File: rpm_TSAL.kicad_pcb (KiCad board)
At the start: 4 copper layers, 123 parts, among them J1 Conn_01x02, J14 Conn_01x04, J2 Conn_01x04, J3 Conn_01x04, J4 Conn_01x04, J6 Conn_01x02, J7 Conn_01x02, Q1 NMOS, Q2 NMOS, Q3 NMOS, Q4 NMOS, Q5 PMOS, Q7 NMOS, U1 OPA355NA, U10 SN74HCS266PWR, U11 OPA355NA, U12 74LVC1G32GV, U13 SFH617A-1X007T, U14 OPA355NA, U15 TBA1-1211E, U16 TBA1-0511E, U17 TBA1-0511E, U18 IP4252CZ16, U2 L7805, U3 74LVC2G74, U4 SFH617A-1X007T, U5 NE555D, U6 CD74HC30PWR, U7 4072, U8 4001, U9 74LVC1G32GV

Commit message: Added Sub project
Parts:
- removed C2, C36, C38, C5, C6, C7: 100nF, Capacitor_SMD:C_0603_1608Metric
- removed C35, C37: 10uF, Capacitor_SMD:C_0603_1608Metric
- removed Q7: NMOS, Package_TO_SOT_SMD:SOT-23-3
- removed R1, R22, R23, R25, R26, R67: 1k, Resistor_SMD:R_0603_1608Metric
- removed R2, R3, R4, R5, R6, R7: 52k3, Resistor_SMD:R_0805_2012Metric
- removed R24: 12k, Resistor_SMD:R_0603_1608Metric
- removed R27, R83: 10k, Resistor_SMD:R_0603_1608Metric
- removed R82: 200R, Resistor_SMD:R_0603_1608Metric
- removed U1: OPA355NA, Package_TO_SOT_SMD:SOT-23-6
- removed U17: TBA1-0511E, Converter_DCDC:Converter_DCDC_TRACO_TBA1-xxxxE_Single_THT
- removed U4: SFH617A-1X007T, Package_DIP:SMDIP-4_W9.53mm_Clearance8mm
- removed U5: NE555D, Package_SO:SOIC-8_3.9x4.9mm_P1.27mm
- added H5: MountingHole, MountingHole:MountingHole_3.2mm_M3, F.Cu at (129.1, 76.5)
- added J10: Conn_01x10, Connector_IDC:IDC-Header_2x05_P2.54mm_Latch6.5mm_Vertical, F.Cu at (174.0, 76.2)
- H1, H2, H3, H4: footprint MountingHole:MountingHole_3.2mm_M3_DIN965 -> MountingHole:MountingHole_3.2mm_M3
- U19, U20, U21: moved to B.Cu
- moved J14 181.8 mm to (188.8, 126.0)
- moved R13 181.7 mm to (243.9, 111.7), turned to 90 degrees
- moved R12 181.4 mm to (243.9, 105.3), turned to -90 degrees
- moved R11 181.2 mm to (243.9, 99.3), turned to -90 degrees
- moved R10 181.1 mm to (243.9, 93.3), turned to 90 degrees
- moved R9 181.0 mm to (243.9, 87.3), turned to 90 degrees
- moved R8 181.0 mm to (243.9, 82.2), turned to 90 degrees
- moved C8 169.2 mm to (191.8, 101.4), turned to 90 degrees
- moved J2 168.4 mm to (154.9, 126.2)
- moved U15 168.2 mm to (198.3, 102.8)
- moved C4 168.1 mm to (189.3, 101.4), turned to 90 degrees
- moved C3 167.1 mm to (186.8, 101.4), turned to 90 degrees
- moved C1 166.1 mm to (184.3, 101.4), turned to 90 degrees
- moved C15 166.1 mm to (191.8, 97.4), turned to 90 degrees
- moved U11 166.0 mm to (232.8, 85.5), turned to 180 degrees
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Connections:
- J1 pad 1: HV+ -> HV-
- J1 pad 2: HV- -> HV+
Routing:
- net HV-: track 0.00 -> 27.2 mm
- net Net-(U11-+): track 0.00 -> 11.1 mm
- net Net-(J10-Pin_9): track 0.00 -> 8.90 mm
- net Net-(J10-Pin_3): track 0.00 -> 8.86 mm
- net Net-(J10-Pin_7): track 0.00 -> 8.23 mm
- net Net-(J10-Pin_5): track 0.00 -> 8.14 mm
- net Net-(J10-Pin_2): track 0.00 -> 6.26 mm
- net HV+: track 0.00 -> 5.70 mm
- net Net-(J10-Pin_4): track 0.00 -> 5.53 mm
- net Net-(J10-Pin_8): track 0.00 -> 5.53 mm
- net Net-(J10-Pin_6): track 0.00 -> 4.81 mm
- net Net-(R12-Pad2): track 0.00 -> 4.60 mm
- net Net-(R10-Pad2): track 0.00 -> 4.18 mm
- net Net-(R11-Pad2): track 0.00 -> 4.17 mm
- net Net-(R10-Pad1): track 0.00 -> 4.15 mm
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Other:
- board outline added: 125.3 x 61.3 mm
- board text added: "Isolating Case over LV Section"

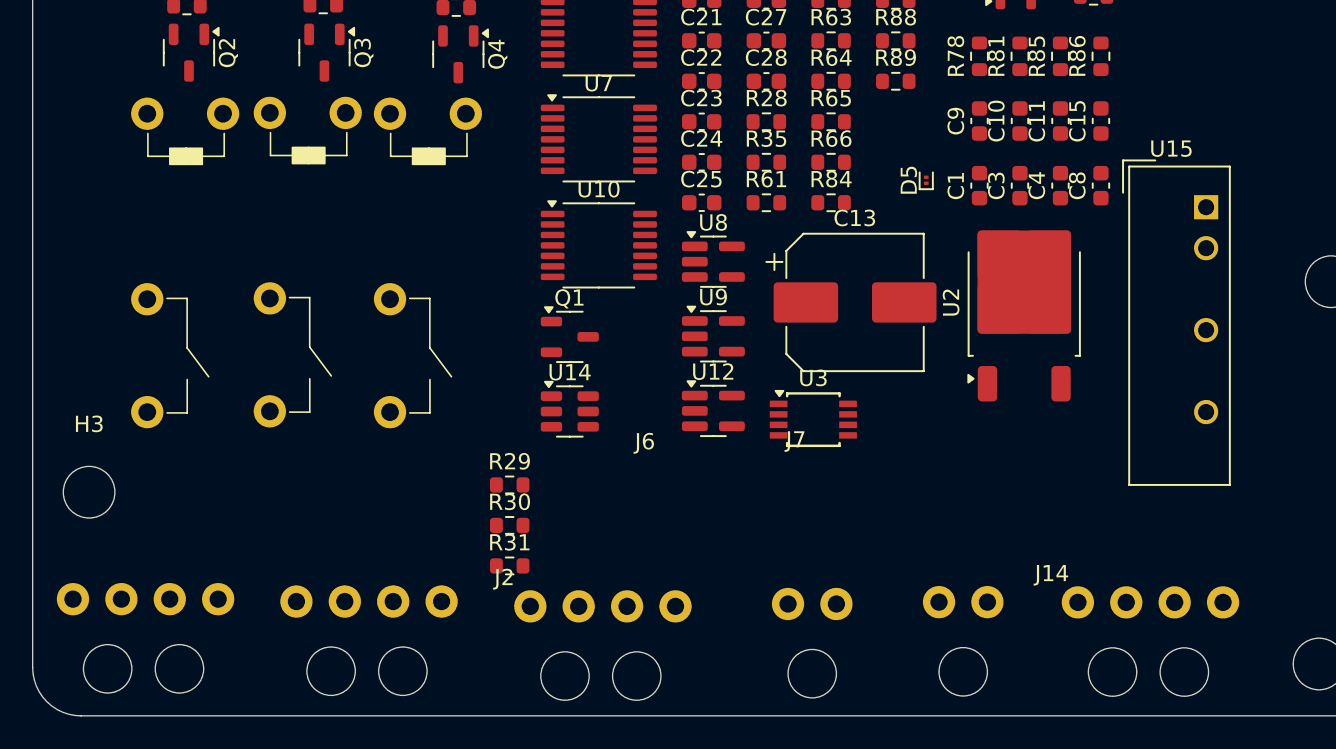
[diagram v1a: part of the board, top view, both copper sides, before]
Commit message: Connector Updated
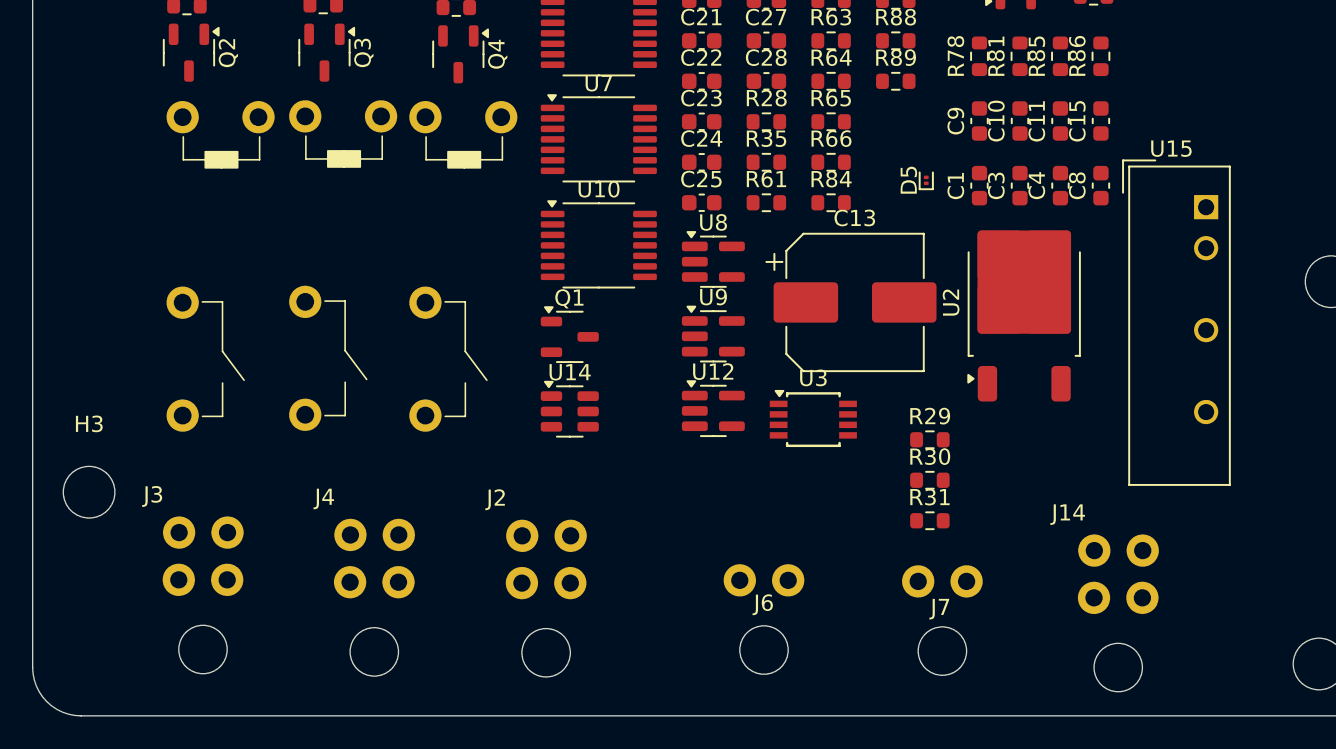
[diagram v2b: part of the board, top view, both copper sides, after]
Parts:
- J14, J2, J3, J4: footprint wuerth_conn:66200411022 -> wuerth_conn:66200421022
- moved R29 26.2 mm to (181.2, 117.2)
- moved R30 26.2 mm to (181.2, 119.7)
- moved R31 26.2 mm to (181.2, 122.2)
- moved J3 8.02 mm to (133.1, 121.2)
- moved J4 5.69 mm to (143.7, 121.3)
- moved J2 4.88 mm to (154.3, 121.4)
- moved J14 3.83 mm to (189.8, 122.3)
- moved J6 3.33 mm to (169.4, 125.9)
- moved U19 2.21 mm to (140.8, 96.2)
- moved U21 2.21 mm to (155.9, 96.2)
- moved U20 2.21 mm to (148.4, 96.1)
- moved J7 1.82 mm to (180.5, 126.0)

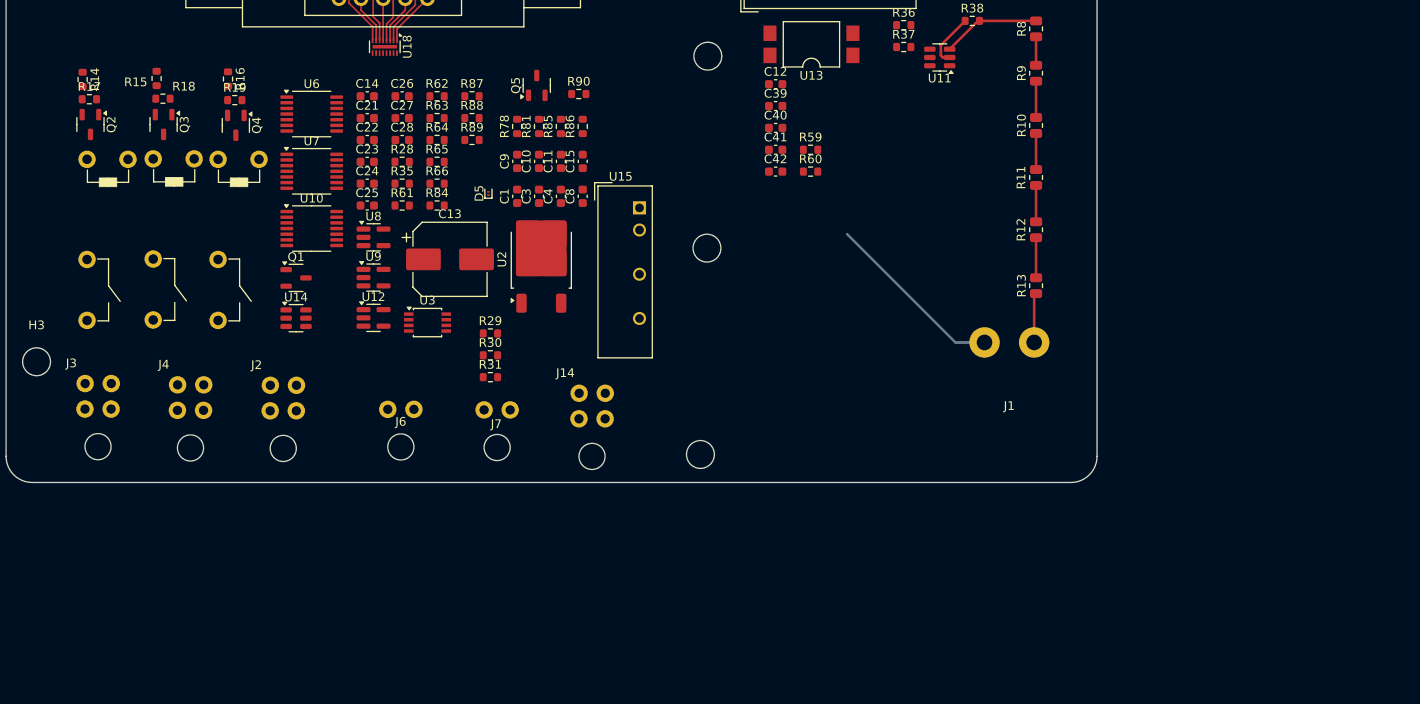
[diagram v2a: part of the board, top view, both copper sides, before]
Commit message: Routing of AIR Relay
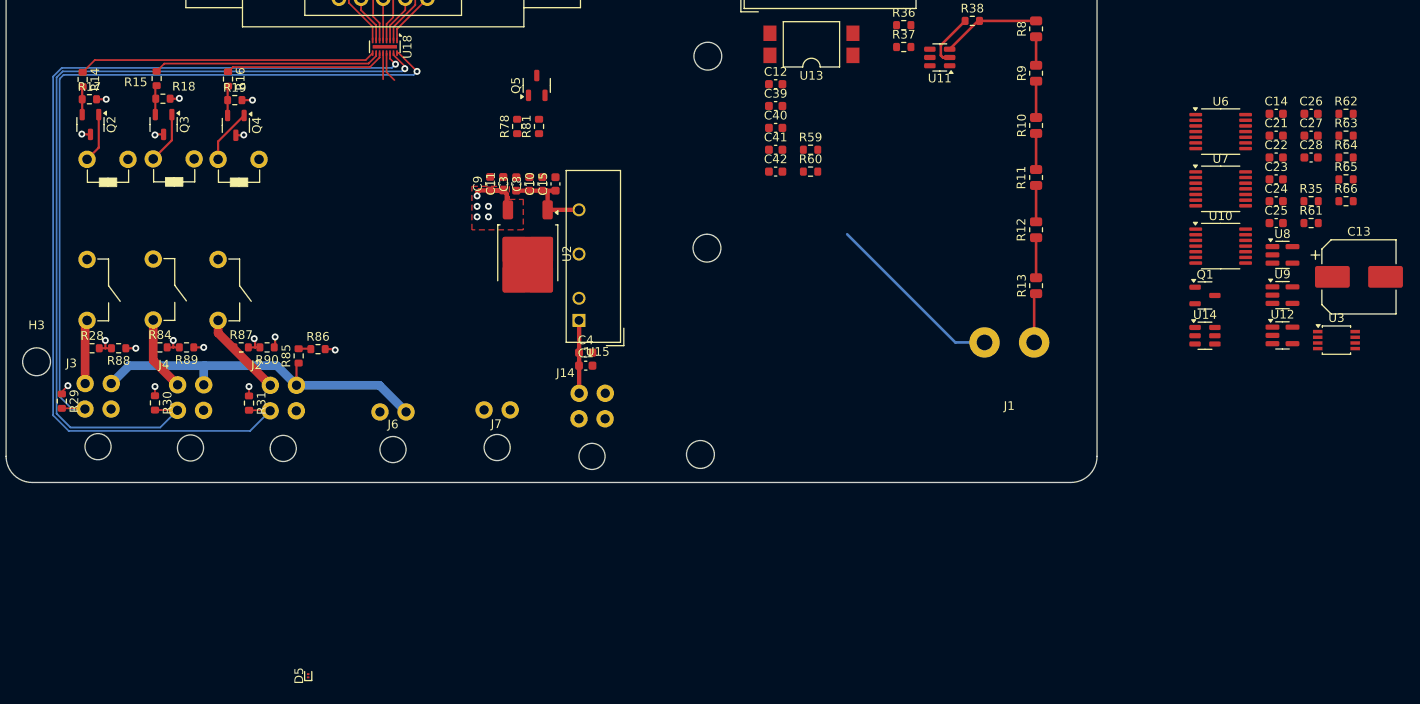
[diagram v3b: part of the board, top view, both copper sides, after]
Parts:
- moved U10 104.4 mm to (265.1, 107.2)
- moved U6 104.4 mm to (265.1, 94.0)
- moved U7 104.4 mm to (265.1, 100.6)
- moved C13 104.4 mm to (281.0, 110.7)
- moved C14 104.4 mm to (271.5, 92.0)
- moved C21 104.4 mm to (271.5, 94.5)
- moved C22 104.4 mm to (271.5, 97.0)
- moved C23 104.4 mm to (271.5, 99.5)
- moved C24 104.4 mm to (271.5, 102.0)
- moved C25 104.4 mm to (271.5, 104.5)
- moved C26 104.4 mm to (275.5, 92.0)
- moved C27 104.4 mm to (275.5, 94.5)
- moved C28 104.4 mm to (275.5, 97.0)
- moved Q1 104.4 mm to (263.3, 112.8)
- moved R35 104.4 mm to (275.5, 102.0)
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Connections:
- J2 pad 1: /LV Connectors/SDC -> /AIR Switch/PRCH_Coil
- J2 pad 2: /AIR Switch/PRCH_Coil -> /LV Connectors/SDC
- J3 pad 1: /LV Connectors/SDC -> /AIR Switch/AIR1_Coil
- J3 pad 2: /AIR Switch/AIR1_Coil -> /LV Connectors/SDC
- J4 pad 1: /LV Connectors/SDC -> /AIR Switch/AIR2_Coil
- J4 pad 2: /AIR Switch/AIR2_Coil -> /LV Connectors/SDC
- U18 pad 11: /AIR Switch/AIR1_SW -> /AIR Switch/PRCH_SW
- U18 pad 9: /AIR Switch/PRCH_SW -> /AIR Switch/AIR1_SW
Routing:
- net /LV Connectors/PRCH_AUX: track 0.00 -> 109.4 mm, vias 0 -> 1
- net /LV Connectors/AIR2_AUX: track 0.00 -> 99.3 mm, vias 0 -> 1
- net /LV Connectors/AIR1_AUX: track 0.00 -> 87.3 mm, vias 0 -> 1
- net /LV Connectors/SDC: track 0.00 -> 41.8 mm
- net /AIR Switch/AIR1_SW: track 0.00 -> 34.2 mm
- net /AIR Switch/AIR2_SW: track 0.00 -> 26.3 mm
- net /AIR Switch/PRCH_SW: track 0.00 -> 18.6 mm
- net GND: track 0.00 -> 11.1 mm, vias 0 -> 10
- net +5V: track 0.00 -> 10.7 mm, vias 0 -> 8
- net +9V: track 0.00 -> 10.3 mm
- net /AIR Switch/PRCH_Coil: track 0.00 -> 9.94 mm
- net /AIR Switch/AIR2_Coil: track 0.00 -> 8.61 mm
- net +24V: track 0.00 -> 8.38 mm
- net /AIR Switch/AIR1_Coil: track 0.00 -> 7.34 mm
- net Net-(Q4-D): track 0.00 -> 6.28 mm
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- added copper zone on F.Cu, net +5V
- added copper zone on In2.Cu, net +5V
- added copper zone on In1.Cu, net GND
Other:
- board text added: "0"
- board text added: "0 mm"
- board text added: "0,01 mm"
- board text added: "0,02"
- board text added: "0,035 mm"
- board text added: "0,1 mm"
- board text added: "1"
- board text added: "1,24 mm"
- board text added: "3,3"
- board text added: "4,5"
- board text added: "B.Cu"
- board text added: "B.Mask"
- board text added: "B.Paste"
- board text added: "B.Silkscreen"
- board text added: "Bottom Silk Screen"
- board text added: "Bottom Solder Mask"
- board text added: "Bottom Solder Paste"
- board text added: "Color"
- board text added: "Dielectric 1"
- board text added: "Dielectric 2"
- board text added: "Dielectric 3"
- board text added: "Epsilon R"
- board text added: "F.Cu"
- board text added: "F.Mask"
- board text added: "F.Paste"
- board text added: "F.Silkscreen"
- board text added: "FR4"
- board text added: "In1.Cu"
- board text added: "In2.Cu"
- board text added: "Layer Name"
- board text added: "Loss Tangent"
- board text added: "Material"
- board text added: "Not specified"
- board text added: "Thickness (mm)"
- board text added: "Top Silk Screen"
- board text added: "Top Solder Mask"
- board text added: "Top Solder Paste"
- board text added: "Type"
- board text added: "copper"
- board text added: "core"
- board text added: "prepreg"

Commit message: misc
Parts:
- removed J14: Conn_01x04, wuerth_conn:66200421022
- added J5: Conn_01x02, wuerth_conn:66200211024, F.Cu at (191.4, 125.9)
- J6: footprint wuerth_conn:66200211024 -> Connector_AMASS:AMASS_XT60-F_1x02_P7.20mm_Vertical
- moved U8 111.7 mm to (161.8, 91.5), turned to 90 degrees
- moved R63 109.2 mm to (171.6, 111.3)
- moved R66 107.2 mm to (173.1, 115.2)
- moved C21 106.5 mm to (165.6, 106.2)
- moved U6 103.8 mm to (161.7, 102.6)
- moved U7 103.5 mm to (161.7, 96.8)
- moved U10 103.2 mm to (161.9, 109.8)
- moved U3 102.1 mm to (176.4, 113.4), turned to -90 degrees
- moved C14 101.4 mm to (173.1, 116.7), turned to 180 degrees
- moved U12 101.3 mm to (171.2, 108.7)
- moved U9 101.0 mm to (171.6, 104.0)
- moved R35 100.2 mm to (175.3, 105.0)
- moved U14 93.6 mm to (169.8, 114.2), turned to 90 degrees
- moved Q1 81.4 mm to (182.0, 115.5)
- moved C13 55.4 mm to (332.9, 129.9)
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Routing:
- net /TSAL Plausibility/TSAL_ERROR: track 3.00 -> 40.9 mm, vias 0 -> 2
- net /LV Connectors/AIR2_AUX: track 99.3 -> 131.9 mm, vias 1 -> 3
- net /LV Connectors/PRCH_AUX: track 109.4 -> 135.7 mm, vias 1 -> 3
- net Net-(R28-Pad2): track 2.30 -> 28.3 mm, vias 1 -> 2
- net Net-(U10-Pad13): track 0.00 -> 23.5 mm, vias 0 -> 2
- net Net-(U6-A): track 0.00 -> 22.2 mm, vias 0 -> 3
- net /LV Connectors/AIR1_AUX: track 87.3 -> 109.1 mm, vias 1 -> 2
- net /LV Connectors/TS_ON: track 3.47 -> 25.2 mm
- net Net-(U6-C): track 0.00 -> 20.8 mm, vias 0 -> 3
- net Net-(R87-Pad2): track 2.37 -> 22.9 mm, vias 1 -> 2
- net Net-(U6-B): track 0.00 -> 20.4 mm, vias 0 -> 3
- net /LV Connectors/SC: track 1.42 -> 21.1 mm
- net Net-(R84-Pad2): track 2.20 -> 19.4 mm, vias 1 -> 2
- net GND: track 11.1 -> 28.0 mm, vias 10 -> 20
- net +5V: track 10.7 -> 26.0 mm, vias 8 -> 17
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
